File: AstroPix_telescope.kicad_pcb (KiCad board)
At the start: 4 copper layers, 84.3 x 96.1 mm, 13 parts, among them J1 AstroPix2_pcie, J2 AstroPix2_pcie, J3 AstroPix2_pcie, J4 AstroPix2_pcie, P1 pcie_GECCO

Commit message: Added Logo + minor improvements
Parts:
- added Logo1: KIT_logo, astropix:logo, F.Cu at (108.3, 126.3)
- P1: footprint Connector_PCBEdge:BUS_PCIexpress_x16 -> astropix:BUS_PCIexpress_x16_mod
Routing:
- net -HV: track 92.8 -> 98.1 mm, vias 2 -> 1
- removed copper zone on B.Cu, net -HV
- removed copper zone on F.Cu, net -HV
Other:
- board text added: "ADL"
- board text added: "AstroPix Telescope 1.0"
- board text added: "Nicolas Striebig 2022"

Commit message: Layout minor improvements
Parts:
- moved R1 4.23 mm to (160.0, 98.7)
- moved R2 1.50 mm to (160.0, 100.6)
- moved R4 1.00 mm to (159.0, 80.3)
- moved R5 0.12 mm to (159.5, 58.8)
- moved R6 0.12 mm to (159.5, 60.7)
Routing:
- net /spi1_miso0: track 42.7 -> 44.7 mm, vias 2 -> 1
- net /spi2_miso1: track 41.3 -> 40.2 mm
- net /spi1_miso1: track 41.0 -> 41.7 mm, vias 2 -> 1
- net GND: track 5.92 -> 5.35 mm

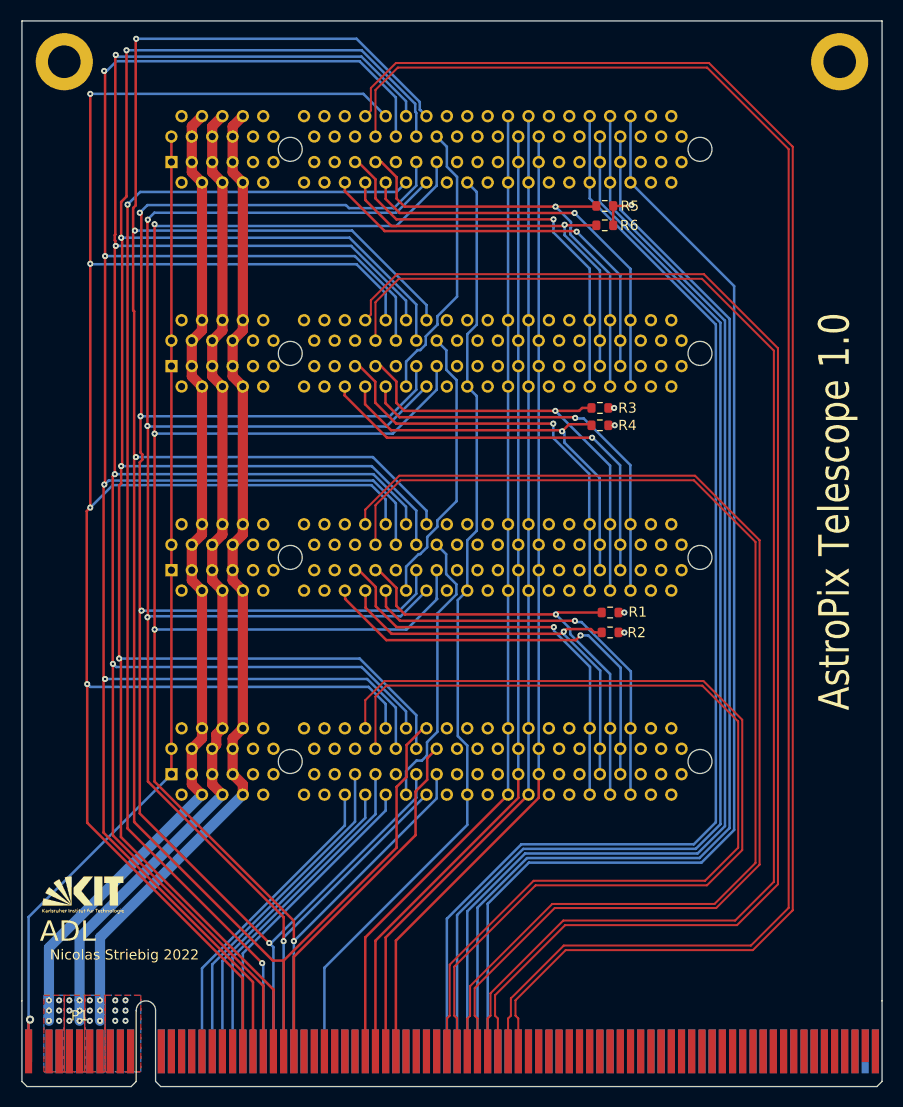
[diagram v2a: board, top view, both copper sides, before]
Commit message: Added signal thPMOS, viastitching and removed unused rings
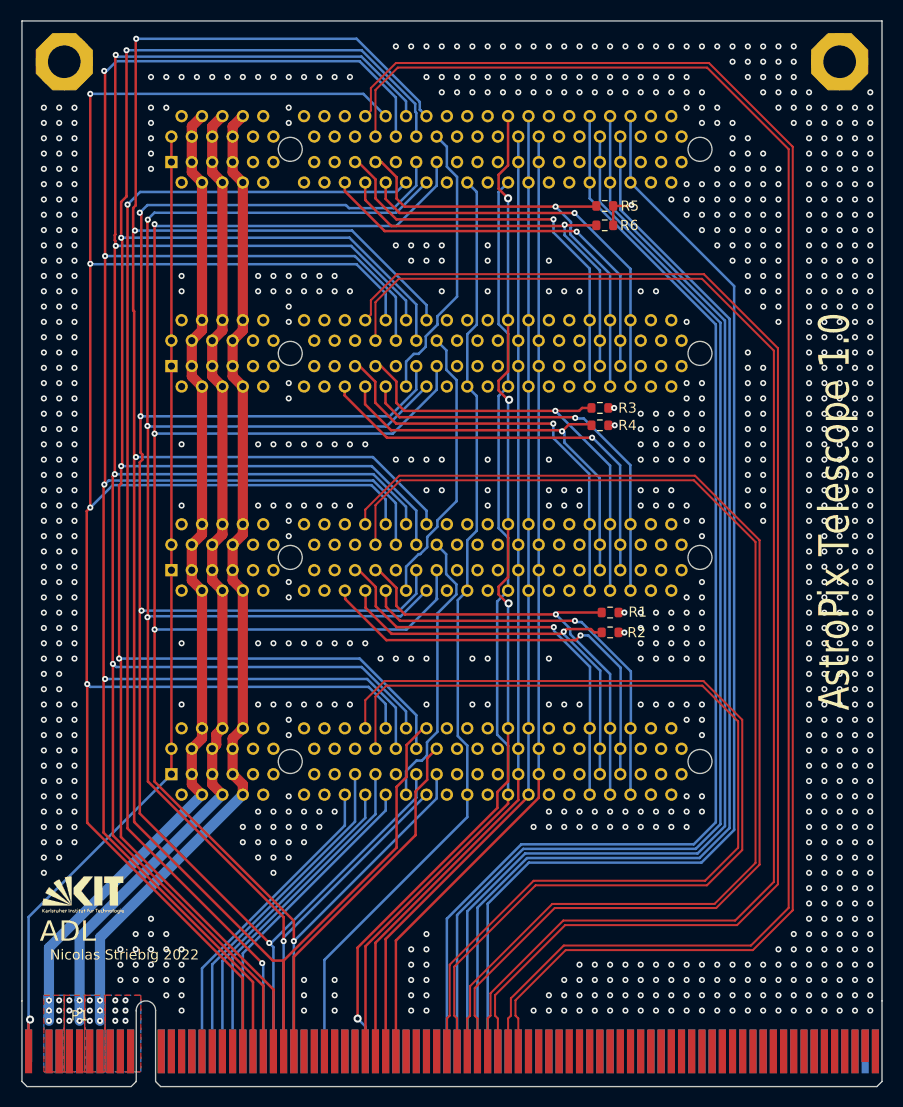
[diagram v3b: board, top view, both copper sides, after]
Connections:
- J1 pad B32: /DAC_blpix -> /DAC_ThPMOS
- J2 pad B32: /DAC_blpix -> /DAC_ThPMOS
- J3 pad B32: /DAC_blpix -> /DAC_ThPMOS
- J4 pad B32: /DAC_blpix -> /DAC_ThPMOS
- P1 pad A32: unconnected-(P1-PadA32) -> /DAC_ThPMOS
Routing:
- net /DAC_ThPMOS: track 0.00 -> 100.7 mm, vias 0 -> 4
- net /DAC_blpix: track 97.5 -> 93.4 mm
- net GND: vias 11 -> 970

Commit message: Added VSSA for Astropix3
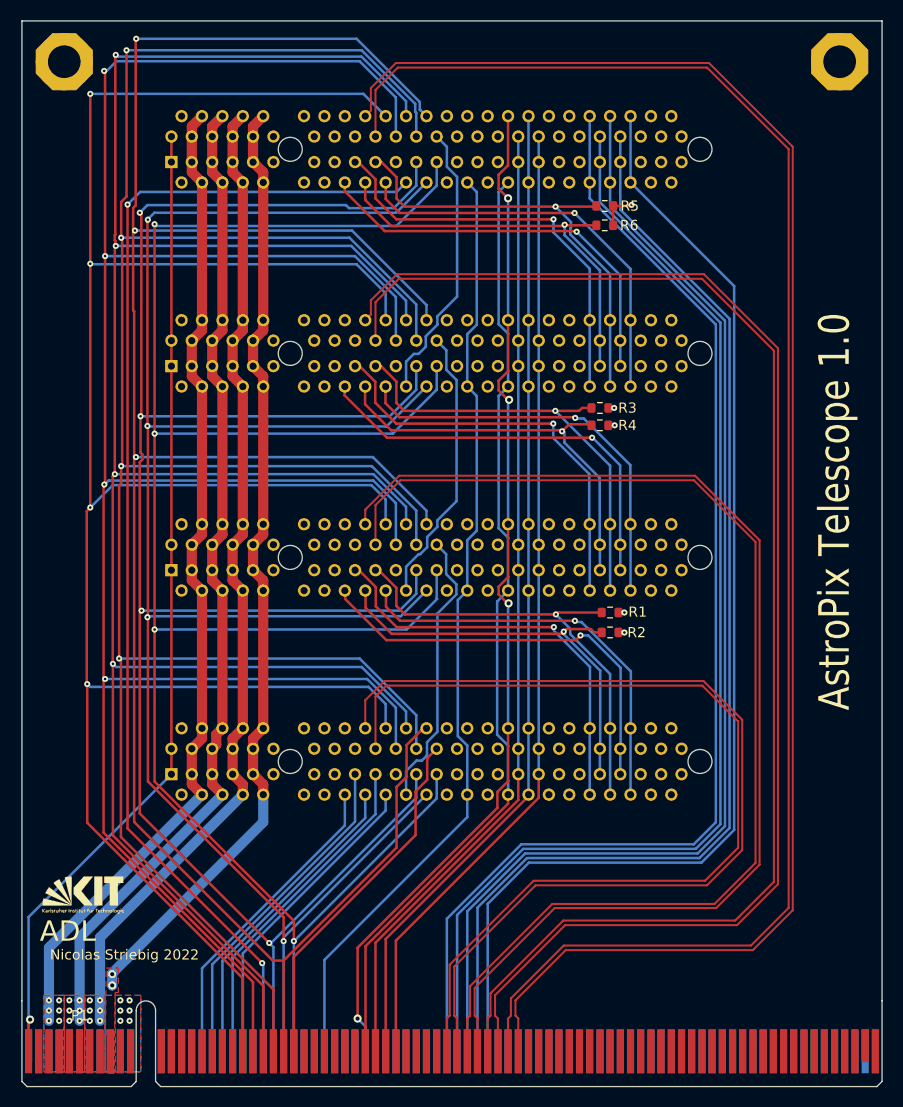
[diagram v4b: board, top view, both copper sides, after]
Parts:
- P1: footprint astropix:BUS_PCIexpress_x16_mod -> Connector_PCBEdge:BUS_PCIexpress_x16
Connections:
- J1 pad A10: (no net) -> VSSA
- J1 pad A9: (no net) -> VSSA
- J1 pad B10: (no net) -> VSSA
- J1 pad B9: (no net) -> VSSA
- J2 pad A10: (no net) -> VSSA
- J2 pad A9: (no net) -> VSSA
- J2 pad B10: (no net) -> VSSA
- J2 pad B9: (no net) -> VSSA
- J3 pad A10: (no net) -> VSSA
- J3 pad A9: (no net) -> VSSA
- J3 pad B10: (no net) -> VSSA
- J3 pad B9: (no net) -> VSSA
- J4 pad A10: (no net) -> VSSA
- J4 pad A9: (no net) -> VSSA
- J4 pad B10: (no net) -> VSSA
- J4 pad B9: (no net) -> VSSA
- P1 pad B10: unconnected-(P1-PadB10) -> VSSA
- P1 pad B9: unconnected-(P1-PadB9) -> VSSA
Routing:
- net VSSA: track 0.00 -> 94.6 mm, vias 0 -> 2
- net GND: vias 970 -> 11
- added copper zone on F.Cu, net VSSA

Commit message: Applied most of corrections.
And re-verified the 100 Ohm characteristic impedance.
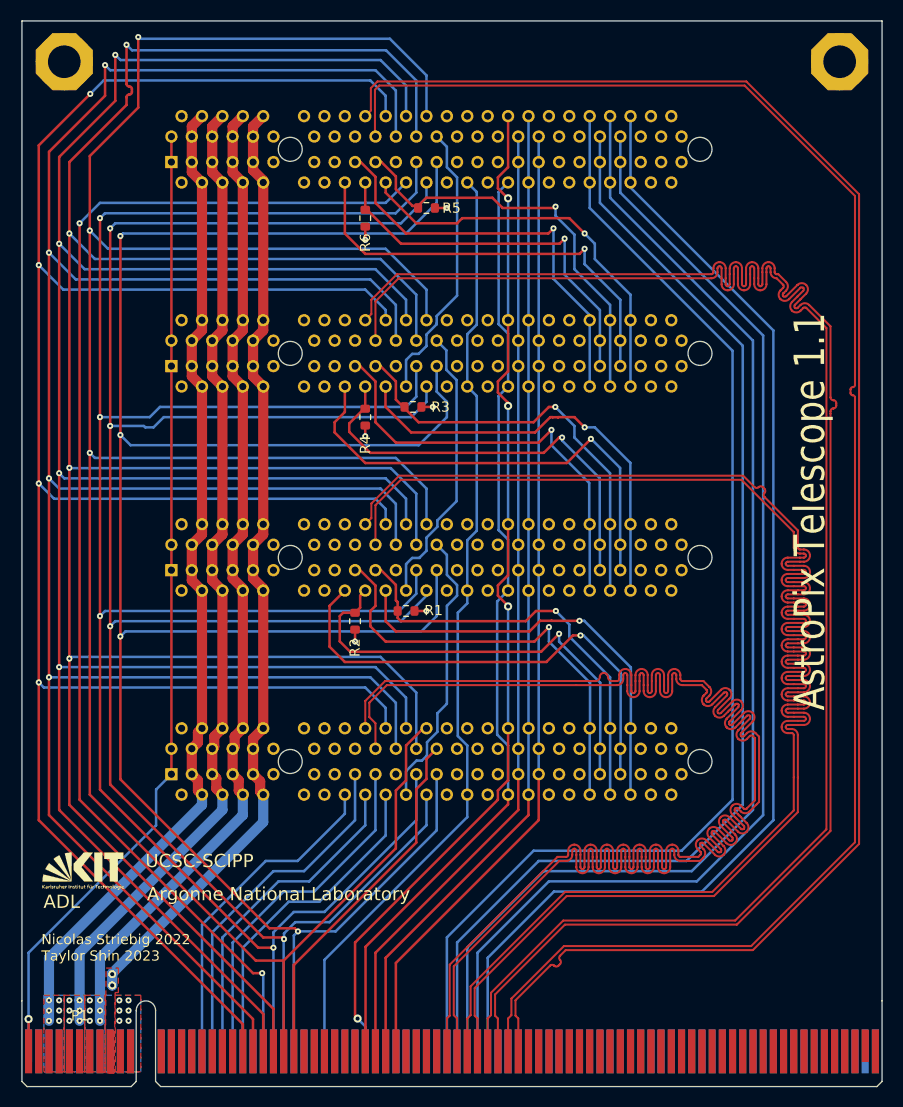
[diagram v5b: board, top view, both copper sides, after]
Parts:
- moved R2 25.0 mm to (135.0, 99.5), turned to -90 degrees
- moved R6 23.5 mm to (136.0, 60.0), turned to -90 degrees
- moved R4 23.0 mm to (136.0, 79.5), turned to -90 degrees
- moved R1 20.0 mm to (140.0, 98.5)
- moved R3 18.3 mm to (140.7, 78.5)
- moved R5 17.5 mm to (142.0, 59.0)
- moved Logo1 2.35 mm to (108.3, 124.0)
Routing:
- net /sample_clk0_P: track 96.2 -> 163.7 mm
- net /sample_clk0_N: track 96.6 -> 163.8 mm
- net /sample_clk2_P: track 115.1 -> 164.4 mm
- net /sample_clk2_N: track 115.6 -> 164.3 mm
- net /sample_clk3_P: track 136.5 -> 164.8 mm
- net /sample_clk3_N: track 136.9 -> 164.6 mm
- net /res_n: track 242.5 -> 267.2 mm
- net /interrupt: track 232.3 -> 255.0 mm
- net /timestamp_clk: track 238.4 -> 259.5 mm
- net /sr_ck2: track 204.1 -> 223.6 mm
- net /hold: track 228.3 -> 246.7 mm
- net /sr_ld: track 231.6 -> 249.4 mm
- net /sr_ck1: track 193.3 -> 210.8 mm
- net /sr_rb: track 201.5 -> 218.2 mm
- net /spi1_csn: track 41.4 -> 47.8 mm
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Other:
- board text added: "Argonne National Laboratory"
- board text added: "AstroPix Telescope 1.1"
- board text added: "Nicolas Striebig 2022 Taylor Shin 2023"
- board text added: "UCSC-SCIPP"
- board text added: "layer {dblquote}F.Silkscreen{dblquote} type {dblquote}Top Silk Screen{dblquote} Color {dblquote}White{dblquote} Material {dblquote}Not specified{dblquote} layer {dblquote}F.Paste{dblquote} type {dblquote}Top Solder Paste{dblquote} layer {dblquote}F.Mask{dblquote} type {dblquote}Top Solder Mask{dblquote} Color {dblquote}Green{dblquote} Thickness 0.01 mm Material {dblquote}Not specified{dblquote} E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"
- board text removed: "AstroPix Telescope 1.0"
- board text removed: "Nicolas Striebig 2022"
